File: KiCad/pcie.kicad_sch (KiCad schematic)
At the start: 34 parts, among them J6 Bus_M.2_Socket_E, J7 Bus_M.2_Socket_E, J8 Bus_PCI_Express_x4, J9 Bus_PCI_Express_x4

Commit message: Begin setting up PCB
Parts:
- J8, J9: footprint Connector_PCBEdge:BUS_PCIexpress_x4 -> EasyEDA2KiCAD:PCIE-TH_AAA-PCI-161-K03
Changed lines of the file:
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@@
 			)
 		)
-		(property "Footprint" "Connector_PCBEdge:BUS_PCIexpress_x4"
+		(property "Footprint" "EasyEDA2KiCAD:PCIE-TH_AAA-PCI-161-K03"
 			(at 440.69 309.88 0)
 			(effects
@@
 			)
 		)
-		(property "Footprint" "Connector_PCBEdge:BUS_PCIexpress_x4"
+		(property "Footprint" "EasyEDA2KiCAD:PCIE-TH_AAA-PCI-161-K03"
 			(at 135.89 303.53 0)
 			(effects

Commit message: Add PCIe x1 Slot
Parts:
- added C347, C349, C350, C353: 100nF/50V, Capacitor_SMD:C_0402_1005Metric, symbol Device:C
- added C348: 10uF/10V, Capacitor_SMD:C_0603_1608Metric, symbol Device:C
- added C351, C352: 100uF/25V, Capacitor_SMD:CP_Elec_6.3x7.7, symbol Device:C_Polarized
- added C354: 560uF/25V, Capacitor_SMD:CP_Elec_6.3x7.7, symbol Device:C_Polarized
- added J17: Bus_PCI_Express_x1, Connector_PCBEdge:BUS_PCIexpress_x1, symbol Connector:Bus_PCI_Express_x1
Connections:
- net +12V: now also C349.1, C350.1, C351.1, C352.1, J17.A2 (+12V), J17.A3 (+12V), J17.B1 (+12V), J17.B2 (+12V), J17.B3 (+12V)
- net +3V3: now also C353.1, C354.1, J17.A10 (+3.3V), J17.A9 (+3.3V), J17.B8 (+3.3V)
- net +3V3SB: now also C347.2, C348.2, J17.B10 (3.3Vaux)
- net GND: now also C347.1, C348.1, C349.2, C350.2, C351.2, C352.2, C353.2, C354.2, J17.A1 (~{PRSNT1}), J17.A12 (GND), J17.A15 (GND), J17.A18 (GND), J17.A4 (GND), J17.B13 (GND), J17.B16 (GND), J17.B17 (~{PRSNT2}), J17.B18 (GND), J17.B4 (GND), J17.B7 (GND)
- net SLOT3_M2E.REFCLK+ renamed SLOT1_M2E.REFCLK+
- net SLOT3_M2E.REFCLK- renamed SLOT1_M2E.REFCLK-
- net SLOT3_M2E.Rx0+ renamed SLOT1_M2E.Rx0+
- net SLOT3_M2E.Rx0- renamed SLOT1_M2E.Rx0-
- net SLOT3_M2E.SUSCLK renamed SLOT1_M2E.SUSCLK
- net SLOT3_M2E.Tx0+ renamed SLOT1_M2E.Tx0+
- net SLOT3_M2E.Tx0- renamed SLOT1_M2E.Tx0-
- net SLOT3_M2E.USB-D+ renamed SLOT1_M2E.USB-D+
- net SLOT3_M2E.USB-D- renamed SLOT1_M2E.USB-D-
- net SLOT3_M2E.~{PLTRST} renamed SLOT1_M2E.~{PLTRST}
- net SLOT3_M2E.~{WAKE} renamed SLOT1_M2E.~{WAKE}
- new net SLOT3x1.REFCLK+: J17.A13 (REFCLK+)
- new net SLOT3x1.REFCLK-: J17.A14 (REFCLK-)
- new net SLOT3x1.Rx0+: J17.A16 (PERp0)
- new net SLOT3x1.Rx0-: J17.A17 (PERn0)
- new net SLOT3x1.SMBCLK: J17.B5 (SMCLK)
- new net SLOT3x1.SMBDAT: J17.B6 (SMDAT)
- new net SLOT3x1.Tx0+: J17.B14 (PETp0)
- new net SLOT3x1.Tx0-: J17.B15 (PETn0)
- new net SLOT3x1.~{PLTRST}: J17.A11 (~{PERST})
- new net SLOT3x1.~{WAKE}: J17.B11 (~{WAKE})
- no-connect marks 94 -> 100
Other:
- moved on the sheet: C139, C140, C141, C142, C143, C144, C145, C146, C147, C148, C151, C152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

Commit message: Finish connecting x1 slot. Add pcie clkreq lines
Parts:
- J17: footprint Connector_PCBEdge:BUS_PCIexpress_x1 -> EasyEDA2KiCAD:CONN-TH_HYCW05-PCI36-155B
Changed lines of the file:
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@@
 			)
 		)
-		(property "Footprint" "Connector_PCBEdge:BUS_PCIexpress_x1"
+		(property "Footprint" "EasyEDA2KiCAD:CONN-TH_HYCW05-PCI36-155B"
 			(at 121.92 298.45 0)
 			(effects

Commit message: Re-annotate schematic
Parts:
- renumbered C139 to C141, C140 to C142, C141 to C143, C142 to C144, C143 to C145, C144 to C146, C145 to C147, C146 to C148, C347 to C149, C348 to C150, C147 to C151, C148 to C152, C149 to C153, C150 to C154, C349 to C155, C350 to C156, C351 to C157, C352 to C158, C353 to C159, C354 to C160, C151 to C161, C152 to C162, C153 to C163, C154 to C164, C155 to C165, C156 to C166, C157 to C167, C158 to C168, C159 to C169, C160 to C170, C161 to C171, C162 to C172, J9 to J10, J17 to J8, J8 to J9, R107 to R100, R104 to R97, R105 to R98, R106 to R99

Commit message: change sata symbols
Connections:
- net GND: no longer J6.53 (~{CLKREQ0}), J7.53 (~{CLKREQ0})
- new net SLOT1_M2E.~{CLKREQ}: J7.53 (~{CLKREQ0})
- new net SLOT2_M2E.~{CLKREQ}: J6.53 (~{CLKREQ0})
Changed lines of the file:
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@@
 	)
 	(bus_entry
+		(at 97.79 76.2)
+		(size 2.54 2.54)
+		(stroke
+			(width 0)
+			(type default)
+		)
+	)
+	(bus_entry
 		(at 481.33 292.1)
 		(size -2.54 2.54)
@@
 	)
 	(bus_entry
+		(at 396.24 68.58)
+		(size 2.54 2.54)
+		(stroke
+			(width 0)
+			(type default)
+		)
+	)
+	(bus_entry
 		(at 481.33 325.12)
 		(size -2.54 2.54)
@@
 	(wire
 		(pts
-			(xy 420.37 71.12) (xy 421.64 71.12)
+			(xy 464.82 262.89) (xy 464.82 271.78)
 		)
 		(stroke
@@
 		)
 	)
-	(wire
+	(bus
 		(pts
-			(xy 464.82 262.89) (xy 464.82 271.78)
+			(xy 97.79 76.2) (xy 97.79 78.74)
 		)
 		(stroke
@@
 	(wire
 		(pts
-			(xy 121.92 78.74) (xy 123.19 78.74)
-		)
-		(stroke
-			(width 0)
-			(type default)
-		)
-	)
-	(wire
-		(pts
 			(xy 455.93 320.04) (xy 478.79 320.04)
 		)
@@
 	(bus
 		(pts
-			(xy 396.24 66.04) (xy 396.24 71.12)
+			(xy 396.24 66.04) (xy 396.24 68.58)
 		)
 		(stroke
@@
 	(wire
 		(pts
+			(xy 398.78 71.12) (xy 421.64 71.12)
+		)
+		(stroke
+			(width 0)
+			(type default)
+		)
+	)
+	(wire
+		(pts
 			(xy 257.81 300.99) (xy 264.16 300.99)
 		)
@@
 	(wire
 		(pts
+			(xy 100.33 78.74) (xy 123.19 78.74)
+		)
+		(stroke
+			(width 0)
+			(type default)
+		)
+	)
+	(wire
+		(pts
 			(xy 434.34 271.78) (xy 429.26 271.78)
 		)
@@
 	(bus
 		(pts
-			(xy 97.79 73.66) (xy 97.79 78.74)
+			(xy 97.79 73.66) (xy 97.79 76.2)
 		)
 		(stroke
@@
 		)
 	)
+	(bus
+		(pts
+			(xy 396.24 68.58) (xy 396.24 71.12)
+		)
+		(stroke
+			(width 0)
+			(type default)
+		)
+	)
 	(wire
 		(pts
@@
 		)
 	)
+	(label "SLOT1_M2E.~{CLKREQ}"
+		(at 101.6 78.74 0)
+		(effects
+			(font
+				(size 1.27 1.27)
+			)
+			(justify left bottom)
+		)
+	)
 	(label "SLOT4x4.Rx0+"
 		(at 295.91 311.15 0)
@@
 		)
 	)
+	(label "SLOT2_M2E.~{CLKREQ}"
+		(at 400.05 71.12 0)
+		(effects
+			(font
+				(size 1.27 1.27)
+			)
+			(justify left bottom)
+		)
+	)
 	(label "SLOT3x1.REFCLK-"
 		(at 88.9 283.21 0)
@@
 	)
 	(symbol
-		(lib_id "power:GND")
-		(at 420.37 71.12 270)
-		(unit 1)
-		(exclude_from_sim no)
-		(in_bom yes)
-		(on_board yes)
-		(dnp no)
-		(property "Reference" "#PWR0121"
-			(at 414.02 71.12 0)
-			(effects
-				(font
-					(size 1.27 1.27)
-				)
-				(hide yes)
-			)
-		)
-		(property "Value" "GND"
-			(at 417.576 70.358 90)
-			(effects
-				(font
-					(size 1.27 1.27)
-				)
-				(justify right)
-			)
-		)
-		(property "Footprint" ""
-			(at 420.37 71.12 0)
-			(effects
-				(font
-					(size 1.27 1.27)
-				)
-				(hide yes)
-			)
-		)
-		(property "Datasheet" ""
-			(at 420.37 71.12 0)
-			(effects
-				(font
-					(size 1.27 1.27)
-				)
-				(hide yes)
-			)
-		)
-		(property "Description" "Power symbol creates a global label with name \"GND\" , ground"
-			(at 420.37 71.12 0)
-			(effects
-				(font
-					(size 1.27 1.27)
-				)
-				(hide yes)
-			)
-		)
-		(pin "1"
-		)
-		(instances
-			(project "LattePandaMuCluster"
-				(path "/49abeb3a-c598-45a3-ba6b-595eb04f17a8/9d5e3449-f80a-40f7-badf-e98b58cab83b"
-					(reference "#PWR0121")
-					(unit 1)
-				)
-			)
-		)
-	)
-	(symbol
 		(lib_id "power:+3V3")
 		(at 146.05 243.84 0)
@@
 					(unit 1)
 				)
-			)
-		)
-	)
-	(symbol
-		(lib_id "power:GND")
-		(at 121.92 78.74 270)
-		(unit 1)
-		(exclude_from_sim no)
-		(in_bom yes)
-		(on_board yes)
-		(dnp no)
-		(property "Reference" "#PWR0122"
-			(at 115.57 78.74 0)
-			(effects
-				(font
-					(size 1.27 1.27)
-				)
-				(hide yes)
-			)
-		)
-		(property "Value" "GND"
-			(at 119.126 77.978 90)
-			(effects
-				(font
-					(size 1.27 1.27)
-				)
-				(justify right)
-			)
-		)
-		(property "Footprint" ""
-			(at 121.92 78.74 0)
-			(effects
-				(font
-					(size 1.27 1.27)
-				)
-				(hide yes)
-			)
-		)
-		(property "Datasheet" ""
-			(at 121.92 78.74 0)
-			(effects
-				(font
-					(size 1.27 1.27)
-				)
-				(hide yes)
-			)
-		)
-		(property "Description" "Power symbol creates a global label with name \"GND\" , ground"
-			(at 121.92 78.74 0)
-			(effects
-				(font
-					(size 1.27 1.27)
-				)
-				(hide yes)
-			)
-		)
-		(pin "1"
-		)
-		(instances
-			(project ""
-				(path "/49abeb3a-c598-45a3-ba6b-595eb04f17a8/9d5e3449-f80a-40f7-badf-e98b58cab83b"
-					(reference "#PWR0122")
-					(unit 1)
-				)

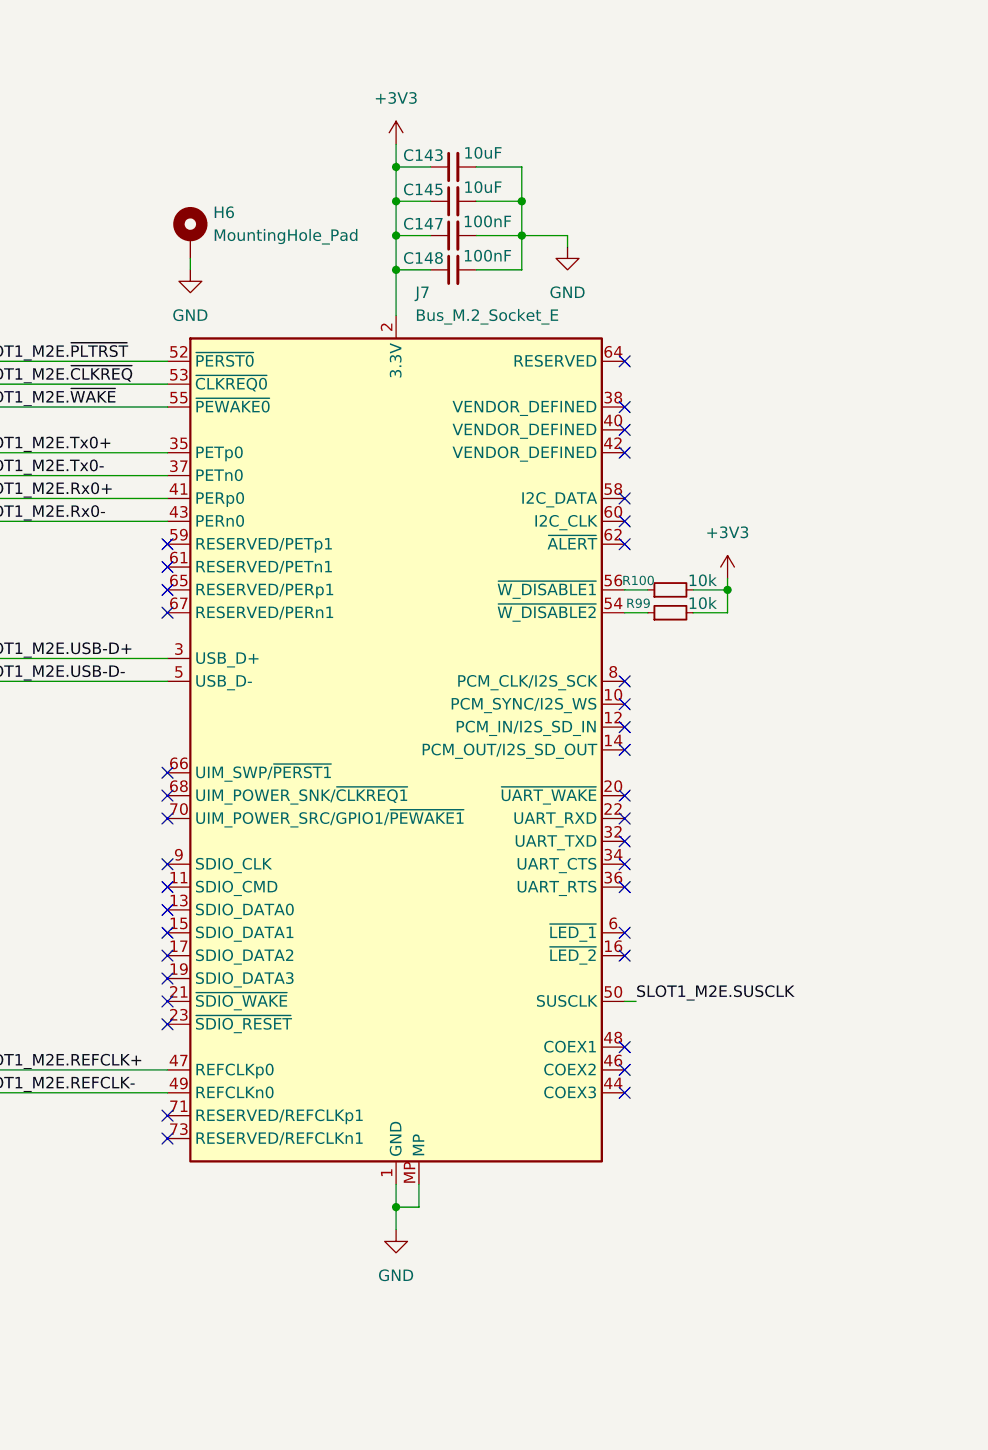
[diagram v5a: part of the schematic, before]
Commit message: Begin moving IO to module sheets
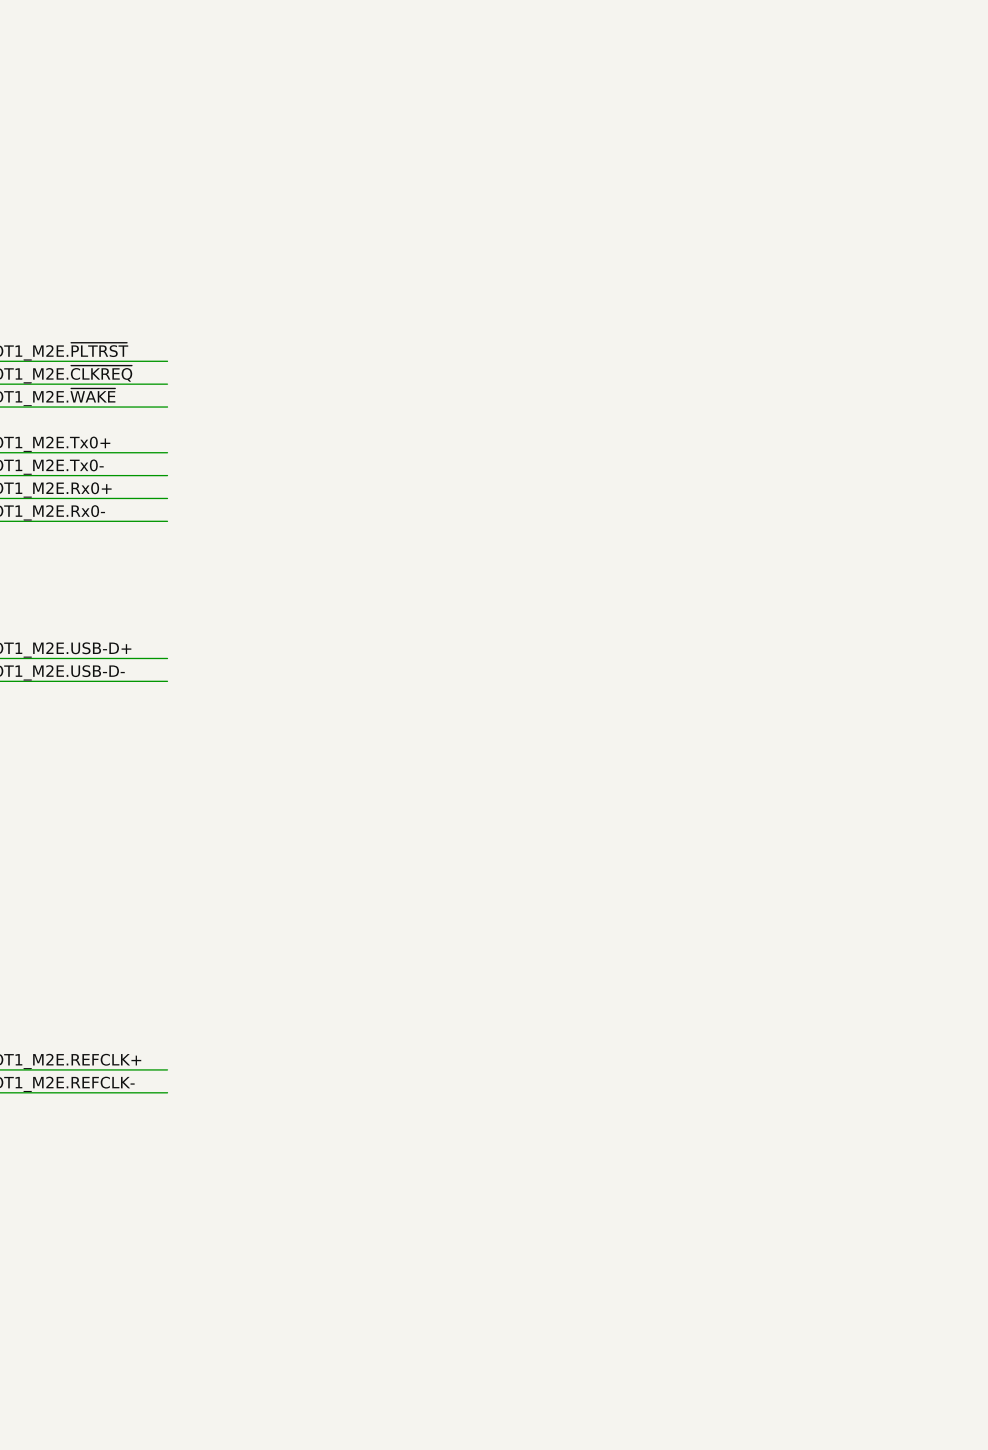
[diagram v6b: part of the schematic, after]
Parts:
- removed C143, C145: 10uF, Capacitor_SMD:C_0603_1608Metric, symbol Device:C_Small
- removed C147, C148: 100nF, Capacitor_SMD:C_0402_1005Metric, symbol Device:C_Small
- removed H6: MountingHole_Pad, MountingHole:MountingHole_2.2mm_M2_Pad_Via, symbol Mechanical:MountingHole_Pad
- removed J7: Bus_M.2_Socket_E, EasyEDA2KiCAD:CONN-SMD_AS0BC21-S48BE-7H, symbol Connector:Bus_M.2_Socket_E
- removed R100, R99: 10k, Resistor_SMD:R_0402_1005Metric, symbol Device:R_Small
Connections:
- no-connect marks 100 -> 62
